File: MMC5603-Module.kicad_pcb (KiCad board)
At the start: 2 copper layers, 29.8 x 15.7 mm, 18 parts, among them CN1 AFC10-S04QCA-00, CN2 AFC10-S04QCA-00, J1 Conn_01x04_Pin, Q1 2N7002KDW, U1 MMC5633NJ, U2 MIC5504-1.8YM5

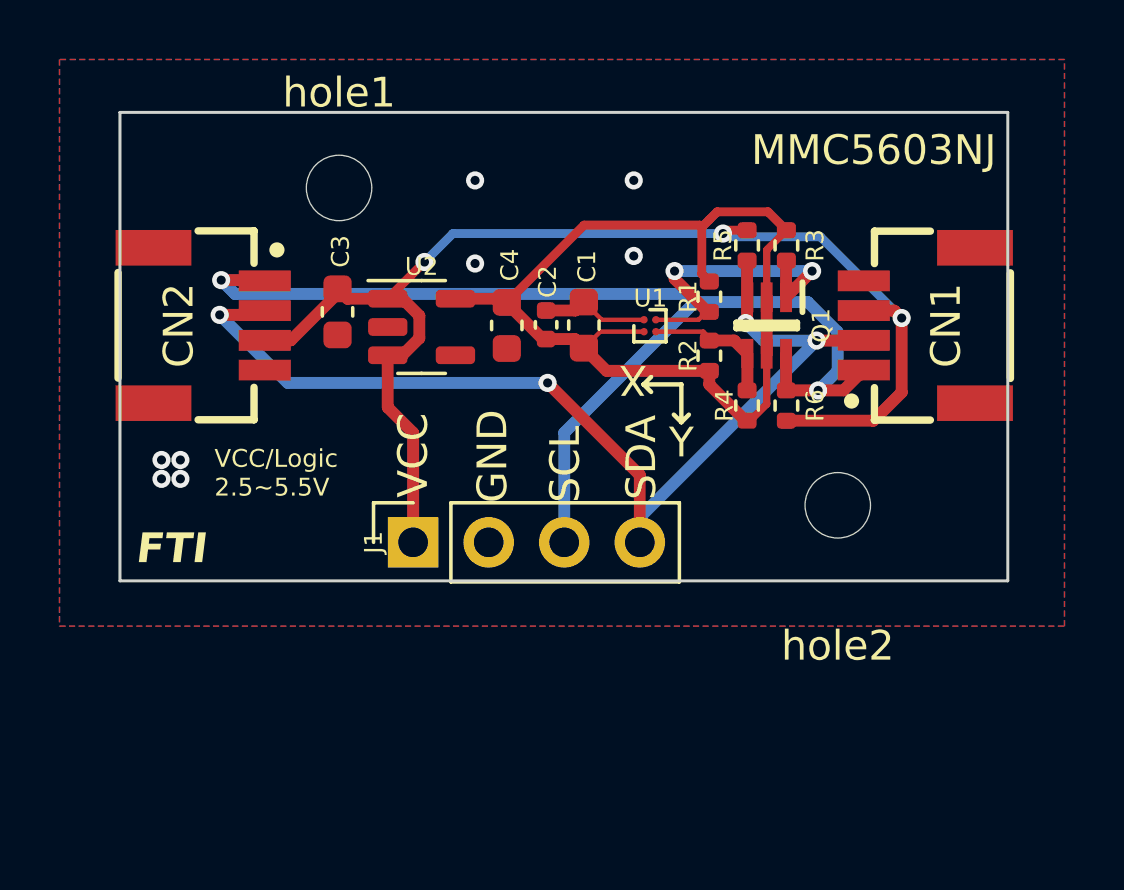
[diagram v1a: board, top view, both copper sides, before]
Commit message: ditch logic shift, fix qwiic pinout, documentation
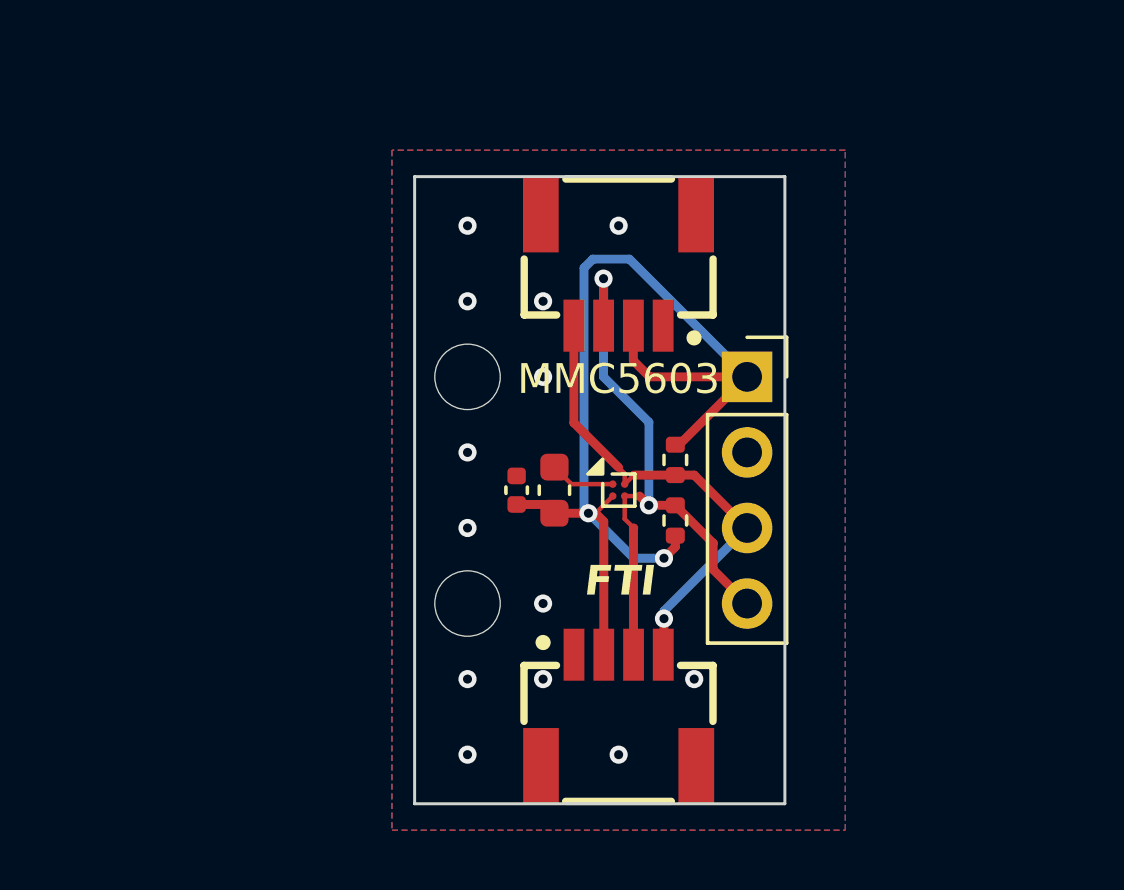
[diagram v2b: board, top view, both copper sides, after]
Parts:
- removed C3, C4: 1u, Capacitor_SMD:C_0603_1608Metric
- removed Q1: 2N7002KDW, 2n7002:SOT65P210X110-6N
- removed R3, R4, R5, R6: 2.2k, Resistor_SMD:R_0402_1005Metric
- removed U2: MIC5504-1.8YM5, Package_TO_SOT_SMD:SOT-23-5
- removed hole1, hole2: MountingHole_2.2mm_M2, MountingHole:MountingHole_2.2mm_M2
- added H1: MountingHole, MountingHole:MountingHole_2.2mm_M2, F.Cu at (147.3, 99.1)
- added H2: MountingHole, MountingHole:MountingHole_2.2mm_M2, F.Cu at (147.3, 106.7)
- U1: value MMC5633NJ -> MMC5603NJ
- moved CN2 18.9 mm to (152.4, 110.3), turned to 0 degrees
- moved J1 12.5 mm to (156.7, 99.1), turned to 0 degrees
- moved CN1 10.3 mm to (152.4, 95.5), turned to 180 degrees
- moved R2 5.66 mm to (154.3, 103.9)
- moved C2 5.65 mm to (149.0, 102.9)
- moved C1 5.64 mm to (150.2, 102.9)
- moved U1 5.62 mm to (152.4, 102.9)
- moved R1 5.60 mm to (154.3, 101.9)
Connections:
- C1 pad 1: +1V8 -> VCC
- C2 pad 1: +1V8 -> VCC
- CN1 pad 1: /SCL -> GND
- CN1 pad 2: /SDA -> VCC
- CN1 pad 3: VCC -> /SDA
- CN1 pad 4: GND -> /SCL
- CN1 pad 5: unconnected-(CN1-Pad5) -> GND
- CN1 pad 6: unconnected-(CN1-Pad6) -> GND
- CN2 pad 1: /SCL -> GND
- CN2 pad 2: /SDA -> VCC
- CN2 pad 3: VCC -> /SDA
- CN2 pad 4: GND -> /SCL
- CN2 pad 5: unconnected-(CN2-Pad5) -> GND
- CN2 pad 6: unconnected-(CN2-Pad6) -> GND
- R1 pad 1: +1V8 -> VCC
- R1 pad 2: /MSCL -> /SCL
- R2 pad 1: +1V8 -> VCC
- R2 pad 2: /MSDA -> /SDA
- U1 pad A2: /MSCL -> /SCL
- U1 pad B1: +1V8 -> VCC
- U1 pad B2: /MSDA -> /SDA
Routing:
- net +1V8: track 33.9 -> 0.00 mm
- net /SCL: track 39.2 -> 16.4 mm, vias 2 -> 1
- net /SDA: track 35.9 -> 21.4 mm, vias 4 -> 2
- net /MSCL: track 10.9 -> 0.00 mm, vias 2 -> 0
- net VCC: track 43.4 -> 36.7 mm, vias 3 -> 2
- net /MSDA: track 4.58 -> 0.00 mm
- net GND: track 3.65 -> 2.20 mm, vias 8 -> 13
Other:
- board size 29.8 x 15.7 mm -> 12.4 x 21.1 mm
- board text added: "MMC5603"
- board text removed: "MMC5603NJ"
- board text removed: "VCC/Logic 2.5~5.5V"
- board text removed: "X"
- board text removed: "Y"
